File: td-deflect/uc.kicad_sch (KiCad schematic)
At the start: 23 parts, among them J4 Conn_ARM_JTAG_SWD_10, J6 Conn_01x06_Male, U12 LM1117-5.0, U2 STM32G474RETx, U23 TPS70933, U25 FM24C64B, U4 TPS70933, U8 INA181, X1 SG-8002CA

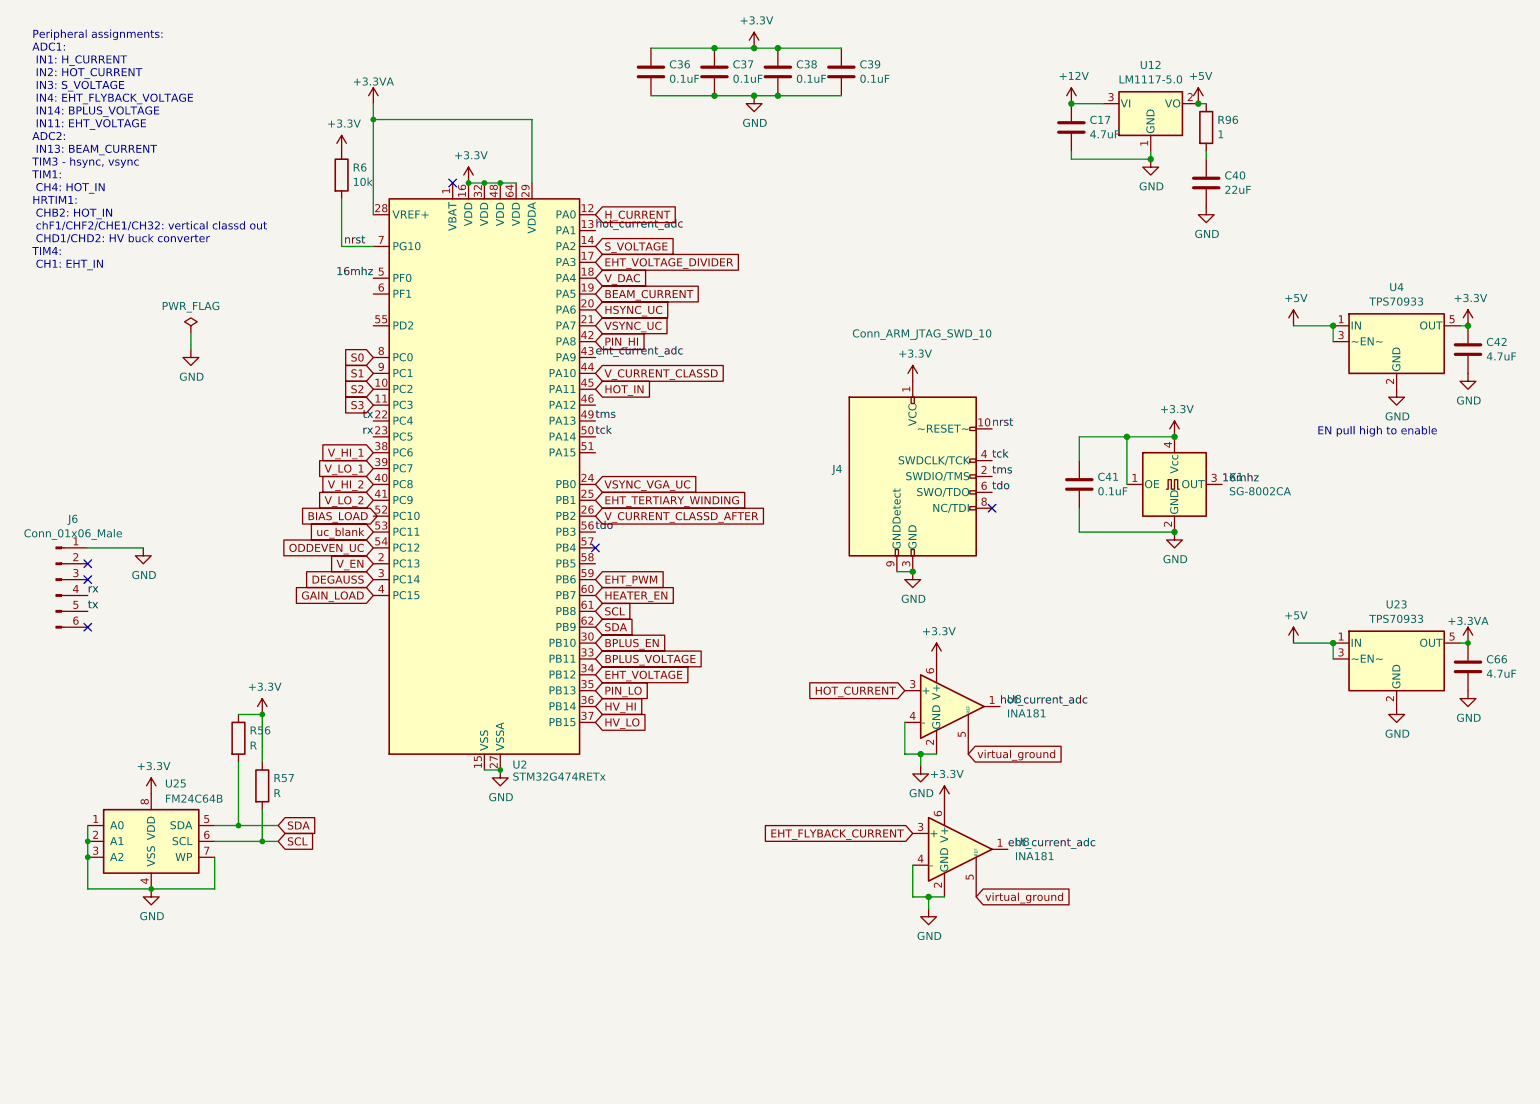
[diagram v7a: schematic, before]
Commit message: switch to 100 pin tqfp microcontroller
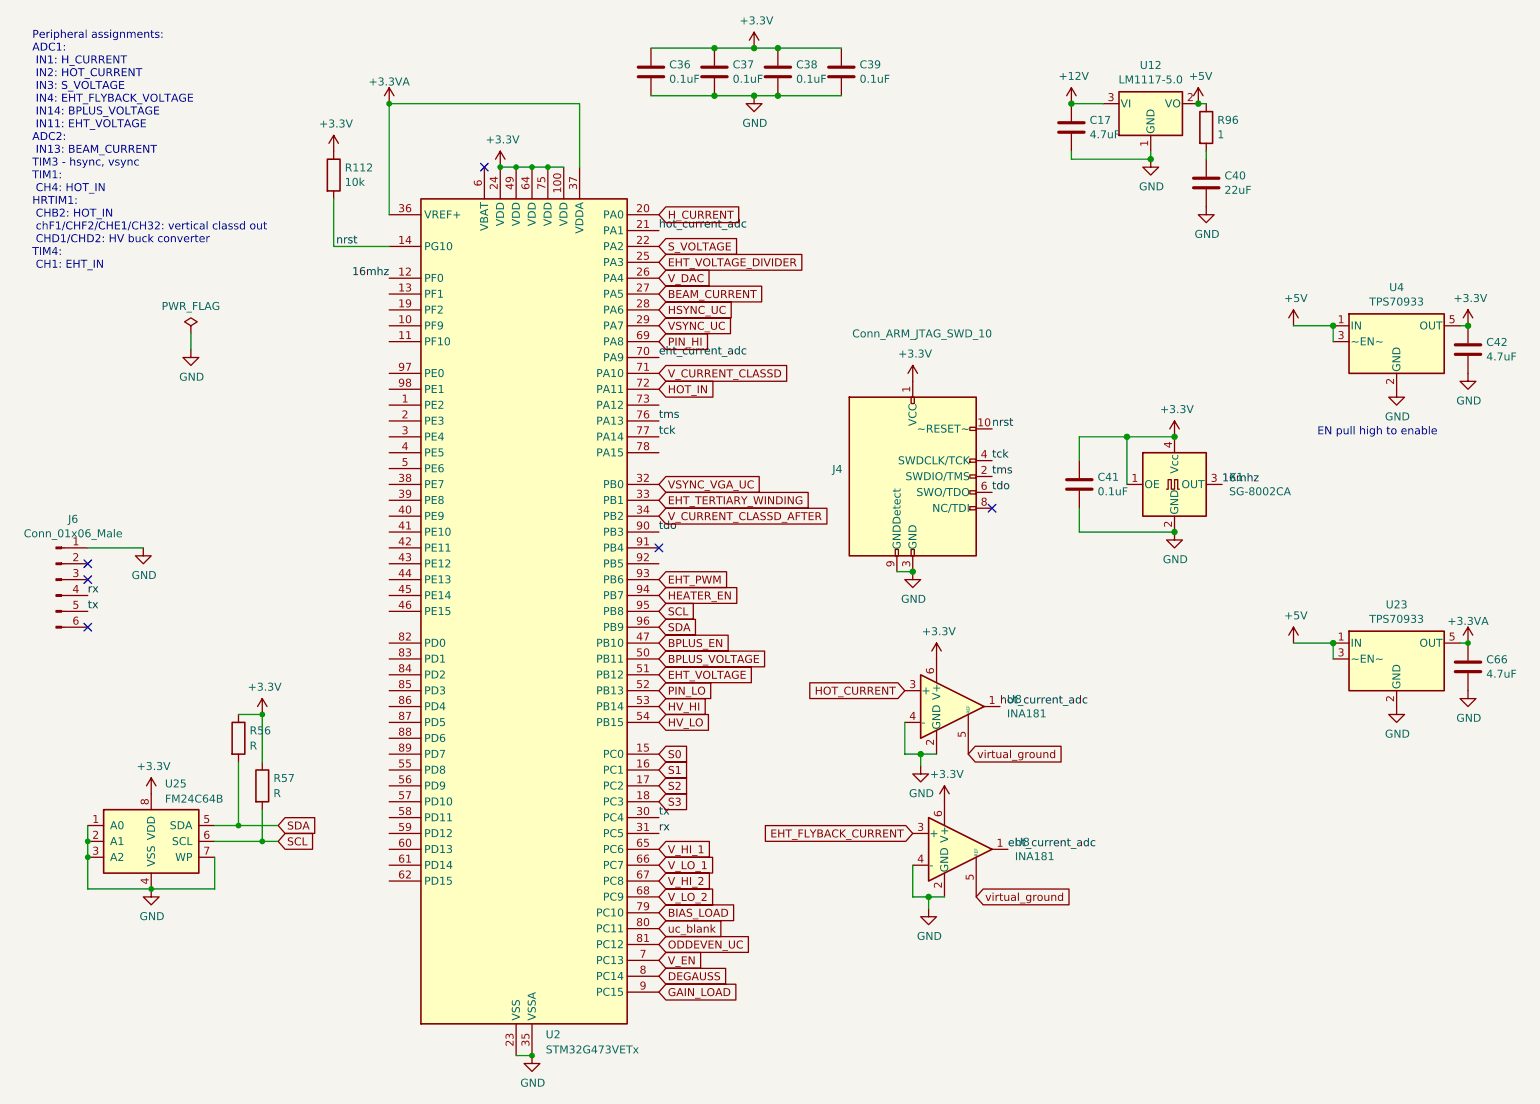
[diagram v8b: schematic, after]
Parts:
- removed R6: 10k, Resistor_SMD:R_0805_2012Metric_Pad1.20x1.40mm_HandSolder, symbol Device:R
- removed U2: STM32G474RETx, Package_QFP:LQFP-64_10x10mm_P0.5mm, symbol MCU_ST_STM32G4:STM32G474RETx
- added R112: 10k, Resistor_SMD:R_0805_2012Metric_Pad1.20x1.40mm_HandSolder, symbol Device:R
- added U2: STM32G473VETx, Package_QFP:LQFP-100_14x14mm_P0.5mm, symbol MCU_ST_STM32G4:STM32G473VETx
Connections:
- net +3.3VA: now also U2.36 (VREF+), U2.37 (VDDA)
- net +3V3: now also R112.1, U2.100 (VDD), U2.24 (VDD), U2.49 (VDD), U2.64 (VDD), U2.75 (VDD)
- net 16mhz: now also U2.12 (PF0)
- net BEAM_CURRENT: now also U2.27 (PA5)
- net BIAS_LOAD: now also U2.79 (PC10)
- net BPLUS_EN: now also U2.47 (PB10)
- net BPLUS_VOLTAGE: now also U2.50 (PB11)
- net DEGAUSS: now also U2.8 (PC14)
- net EHT_PWM: now also U2.93 (PB6)
- net EHT_TERTIARY_WINDING: now also U2.33 (PB1)
- net EHT_VOLTAGE: now also U2.51 (PB12)
- net EHT_VOLTAGE_DIVIDER: now also U2.25 (PA3)
- net GAIN_LOAD: now also U2.9 (PC15)
- net GND: now also U2.23 (VSS), U2.35 (VSSA), U2.48 (VSS), U2.63 (VSS), U2.74 (VSS), U2.99 (VSS)
- net HEATER_EN: now also U2.94 (PB7)
- net HOT_IN: now also U2.72 (PA11)
- net HSYNC_UC: now also U2.28 (PA6)
- net HV_HI: now also U2.53 (PB14)
- net HV_LO: now also U2.54 (PB15)
- net H_CURRENT: now also U2.20 (PA0)
- net ODDEVEN_UC: now also U2.81 (PC12)
- net PIN_HI: now also U2.69 (PA8)
- net PIN_LO: now also U2.52 (PB13)
- net S0: now also U2.15 (PC0)
- net S1: now also U2.16 (PC1)
- net S2: now also U2.17 (PC2)
- net S3: now also U2.18 (PC3)
- net SCL: now also U2.95 (PB8)
- net SDA: now also U2.96 (PB9)
- net S_VOLTAGE: now also U2.22 (PA2)
- net VSYNC_UC: now also U2.29 (PA7)
- net VSYNC_VGA_UC: now also U2.32 (PB0)
- net V_CURRENT_CLASSD: now also U2.71 (PA10)
- net V_CURRENT_CLASSD_AFTER: now also U2.34 (PB2)
- net V_DAC: now also U2.26 (PA4)
- net V_EN: now also U2.7 (PC13)
- net V_HI_1: now also U2.65 (PC6)
- net V_HI_2: now also U2.67 (PC8)
- net V_LO_1: now also U2.66 (PC7)
- net V_LO_2: now also U2.68 (PC9)
- net eht_current_adc: now also U2.70 (PA9)
- net hot_current_adc: now also U2.21 (PA1)
- net nrst: now also R112.2, U2.14 (PG10)
- net rx: now also U2.31 (PC5)
- net tck: now also U2.77 (PA14)
- net tdo: now also U2.90 (PB3)
- net tms: now also U2.76 (PA13)
- net tx: now also U2.30 (PC4)
- net uc_blank: now also U2.80 (PC11)
